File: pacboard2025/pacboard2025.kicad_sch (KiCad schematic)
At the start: 28 parts, among them J1 XT30 Male Connector, U2 D24V50F5, U3 ProS3, U6 BNO085

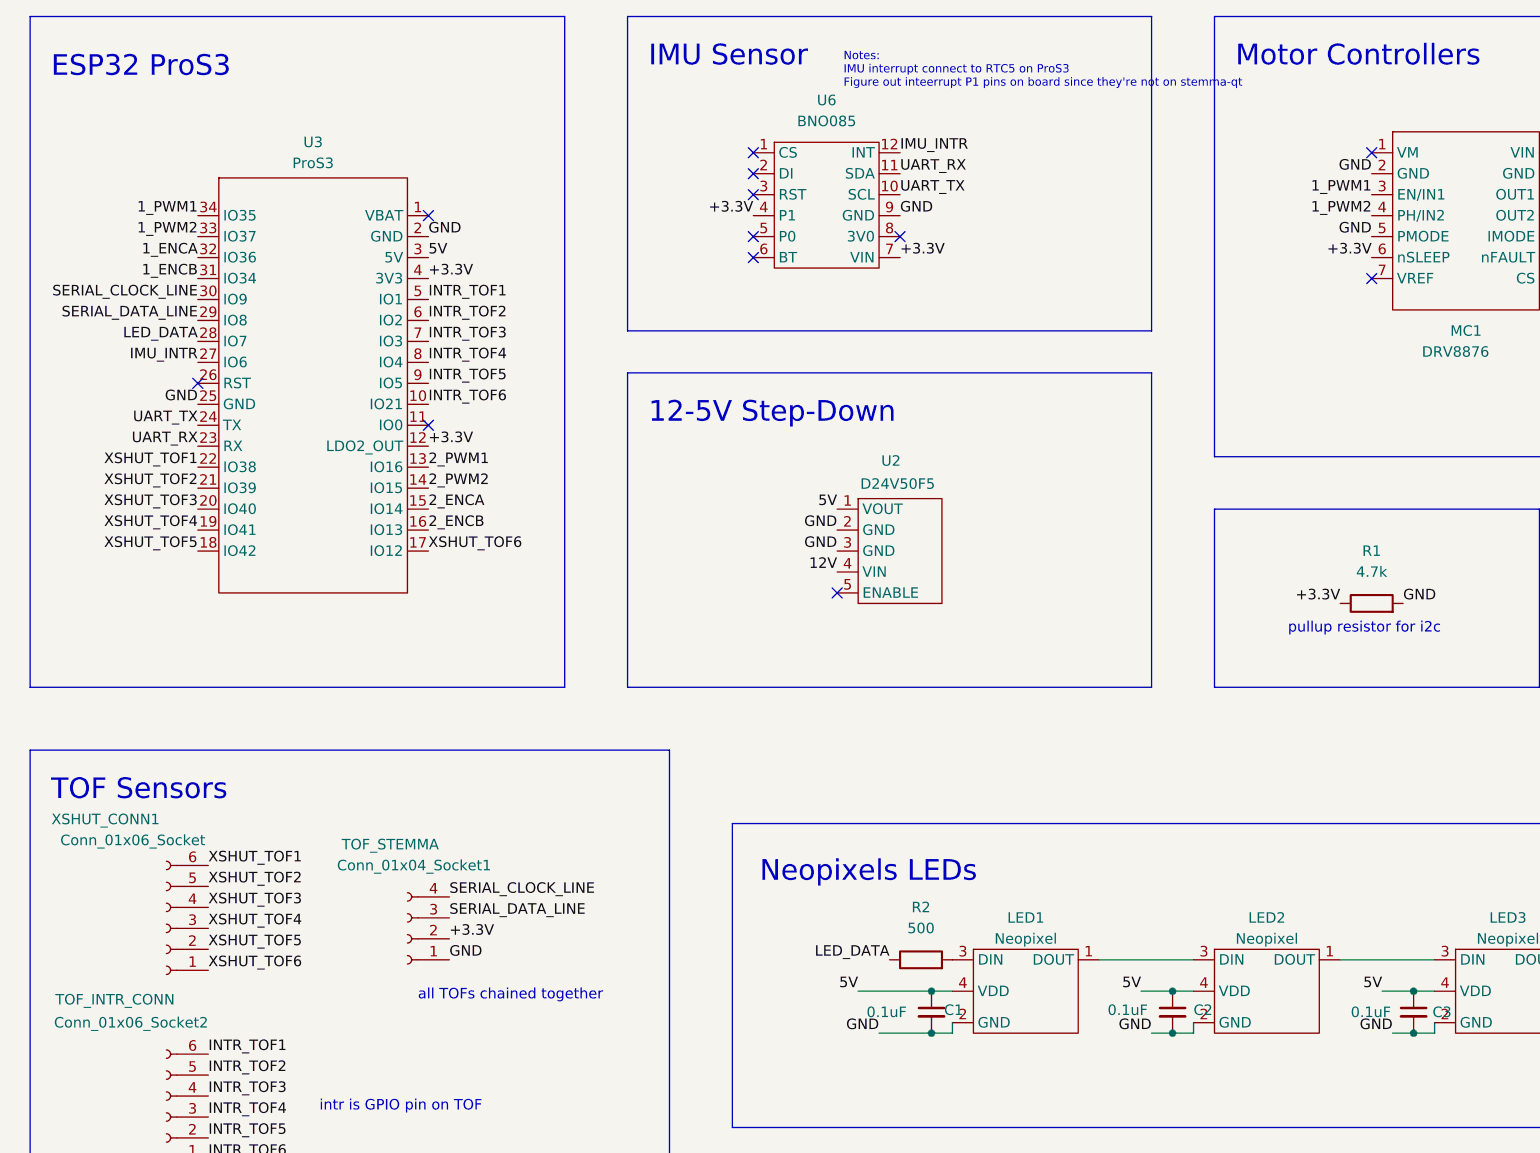
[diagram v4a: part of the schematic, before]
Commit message: changed layout
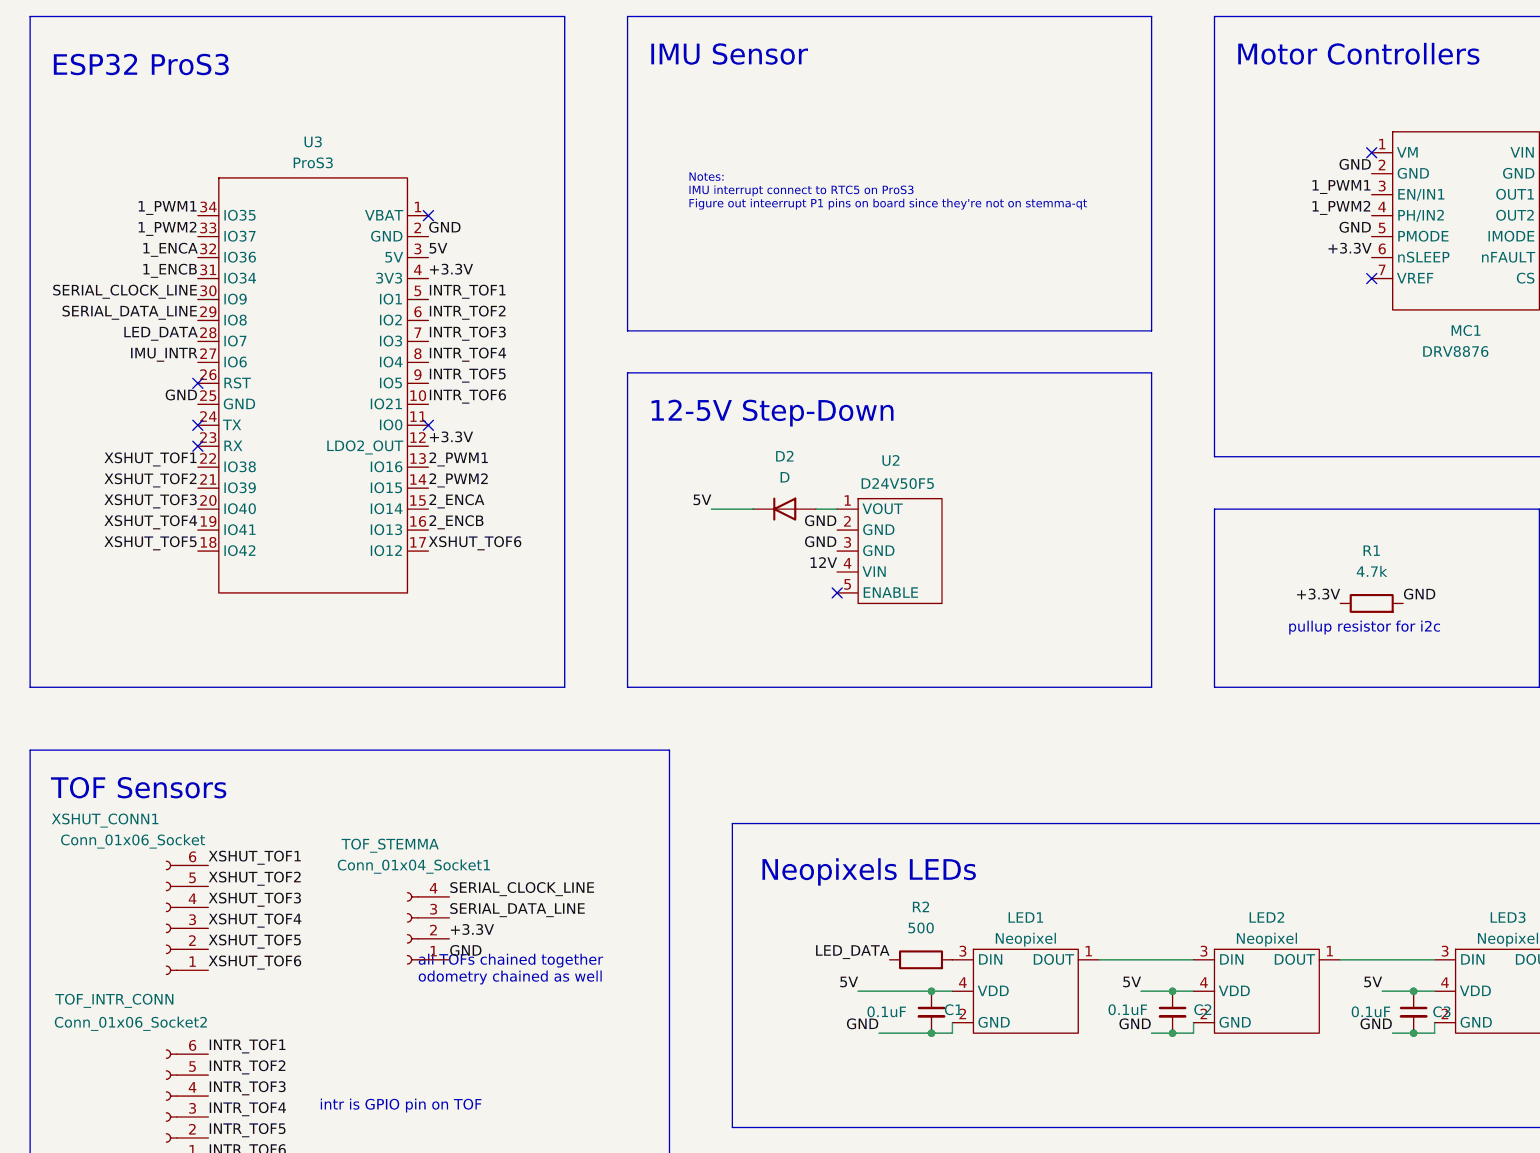
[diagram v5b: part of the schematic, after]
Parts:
- removed U6: BNO085, board1_footprints:BNU0085, symbol board1_libs:BNO085
- added D2: D, Capacitor_SMD:C_0805_2012Metric_Pad1.18x1.45mm_HandSolder, symbol Device:D
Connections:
- net 5V: now also D2.1 (K); no longer U2.1 (VOUT)
- net UART_RX: no longer names the net of U3.23 (RX)
- net UART_TX: no longer names the net of U3.24 (TX)
- new net: D2.2 (A), U2.1 (VOUT)
- no-connect marks 23 -> 19
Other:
- note added: "all TOFs chained together odometry chained as well"
- note removed: "all TOFs chained together"
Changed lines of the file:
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@@
-	)
-	(no_connect
-		(at 109.22 38.1)
 	)
 	(no_connect
@@
 	)
 	(no_connect
+		(at 41.91 71.12)
+	)
+	(no_connect
 		(at 69.85 71.12)
 	)
@@
 	)
 	(no_connect
-		(at 109.22 43.18)
-	)
-	(no_connect
 		(at 259.08 53.34)
-	)
-	(no_connect
-		(at 109.22 48.26)
 	)
 	(no_connect
@@
 	)
 	(no_connect
-		(at 127 48.26)
-	)
-	(no_connect
-		(at 109.22 40.64)
+		(at 41.91 73.66)
 	)
 	(no_connect
@@
 	)
 	(no_connect
-		(at 109.22 50.8)
-	)
-	(no_connect
 		(at 259.08 50.8)
 	)
@@
 	(wire
 		(pts
+			(xy 116.84 81.28) (xy 119.38 81.28)
+		)
+		(stroke
+			(width 0)
+			(type default)
+		)
+	)
+	(wire
+		(pts
 			(xy 214.63 139.7) (xy 218.44 139.7)
 		)
@@
 		(pts
 			(xy 124.46 144.78) (xy 130.81 144.78)
+		)
+		(stroke
+			(width 0)
+			(type default)
+		)
+	)
+	(wire
+		(pts
+			(xy 104.14 81.28) (xy 109.22 81.28)
 		)
 		(stroke
@@
 	(text "Notes:\nIMU interrupt connect to RTC5 on ProS3\nFigure out inteerrupt P1 pins on board since they're not on stemma-qt\n\n"
 		(exclude_from_sim no)
-		(at 120.142 28.956 0)
+		(at 101.346 43.688 0)
 		(effects
 			(font
@@
 		)
 	)
-	(text "all TOFs chained together\n"
+	(text "all TOFs chained together\nodometry chained as well\n\n"
 		(exclude_from_sim no)
 		(at 68.58 140.97 0)
@@
 		)
 	)
-	(label "+3.3V"
-		(at 109.22 45.72 180)
-		(fields_autoplaced yes)
-		(effects
-			(font
-				(size 1.27 1.27)
-			)
-			(justify right bottom)
-		)
-	)
 	(label "BAT_12V"
 		(at 295.91 38.1 0)
@@
 		)
 	)
-	(label "UART_TX"
-		(at 127 43.18 0)
-		(fields_autoplaced yes)
-		(effects
-			(font
-				(size 1.27 1.27)
-			)
-			(justify left bottom)
-		)
-	)
 	(label "XSHUT_TOF6"
 		(at 69.85 86.36 0)
@@
 		)
 	)
-	(label "UART_TX"
-		(at 41.91 71.12 180)
-		(fields_autoplaced yes)
-		(effects
-			(font
-				(size 1.27 1.27)
-			)
-			(justify right bottom)
-		)
-	)
-	(label "+3.3V"
-		(at 127 50.8 0)
-		(fields_autoplaced yes)
-		(effects
-			(font
-				(size 1.27 1.27)
-			)
-			(justify left bottom)
-		)
-	)
 	(label "XSHUT_TOF2"
 		(at 43.18 127 0)
@@
 		)
 	)
-	(label "IMU_INTR"
-		(at 127 38.1 0)
-		(fields_autoplaced yes)
-		(effects
-			(font
-				(size 1.27 1.27)
-			)
-			(justify left bottom)
-		)
-	)
 	(label "XSHUT_TOF6"
 		(at 43.18 137.16 0)
@@
 	)
 	(label "GND"
-		(at 127 45.72 0)
-		(fields_autoplaced yes)
-		(effects
-			(font
-				(size 1.27 1.27)
-			)
-			(justify left bottom)
-		)
-	)
-	(label "GND"
 		(at 69.85 48.26 0)
 		(fields_autoplaced yes)
@@
 		)
 	)
-	(label "UART_RX"
-		(at 127 40.64 0)
-		(fields_autoplaced yes)
-		(effects
-			(font
-				(size 1.27 1.27)
-			)
-			(justify left bottom)
-		)
-	)
 	(label "1_PWM2"
 		(at 184.15 45.72 180)
@@
 		)
 	)
-	(label "UART_RX"
-		(at 41.91 73.66 180)
-		(fields_autoplaced yes)
-		(effects
-			(font
-				(size 1.27 1.27)
-			)
-			(justify right bottom)
-		)
-	)
 	(label "SERIAL_DATA_LINE"
 		(at 41.91 58.42 180)
@@
 	)
 	(label "5V"
-		(at 119.38 81.28 180)
+		(at 104.14 81.28 180)
 		(fields_autoplaced yes)
 		(effects
@@
 	)
 	(symbol
-		(lib_id "board1_libs:BNO085")
-		(at 118.11 35.56 0)
-		(unit 1)
-		(exclude_from_sim no)
-		(in_bom yes)
-		(on_board yes)
-		(dnp no)
-		(fields_autoplaced yes)
-		(property "Reference" "U6"
-			(at 118.11 31.75 0)
-			(effects
-				(font
-					(size 1.27 1.27)
-				)
-			)
-		)
-		(property "Value" "BNO085"
-			(at 118.11 34.29 0)
-			(effects
-				(font
-					(size 1.27 1.27)
-				)
-			)
-		)
-		(property "Footprint" "board1_footprints:BNU0085"
-			(at 118.11 35.56 0)
-			(effects
-				(font
-					(size 1.27 1.27)
-				)
-				(hide yes)
-			)
-		)
-		(property "Datasheet" ""
-			(at 118.11 35.56 0)
-			(effects
-				(font
-					(size 1.27 1.27)
-				)
-				(hide yes)
-			)
-		)
-		(property "Description" ""
-			(at 118.11 35.56 0)
-			(effects
-				(font
-					(size 1.27 1.27)
-				)
-				(hide yes)
-			)
-		)
-		(pin "10"
-		)
-		(pin "11"
-		)
-		(pin "12"
-		)
-		(pin "2"
-		)
-		(pin "3"
-		)
-		(pin "4"
-		)
-		(pin "5"
-		)
-		(pin "6"
-		)
-		(pin "7"
-		)
-		(pin "8"
-		)
-		(pin "9"
-		)
-		(pin "1"
-		)
-		(instances
-			(project "pacboard2025"
-				(path "/8e380e0f-b63e-4626-b5ee-6ded4a9a683b"
-					(reference "U6")
-					(unit 1)
-				)
-			)
-		)
-	)
-	(symbol
 		(lib_id "board1_libs:DRV8876")
 		(at 193.04 36.83 0)
@@
 					(unit 1)
 				)
+			)
+		)
+	)
+	(symbol
+		(lib_id "Device:D")
+		(at 113.03 81.28 0)
+		(unit 1)
+		(exclude_from_sim no)
+		(in_bom yes)
+		(on_board yes)
+		(dnp no)
+		(fields_autoplaced yes)
+		(property "Reference" "D2"
+			(at 113.03 74.93 0)
+			(effects
+				(font
+					(size 1.27 1.27)
+				)
+			)
+		)
+		(property "Value" "D"
+			(at 113.03 77.47 0)
+			(effects
+				(font
+					(size 1.27 1.27)
+				)
+			)
+		)
+		(property "Footprint" "Capacitor_SMD:C_0805_2012Metric_Pad1.18x1.45mm_HandSolder"
+			(at 113.03 81.28 0)
+			(effects
+				(font
+					(size 1.27 1.27)
+				)
+				(hide yes)
+			)
+		)
+		(property "Datasheet" "~"
+			(at 113.03 81.28 0)
+			(effects
+				(font
+					(size 1.27 1.27)
+				)
+				(hide yes)
+			)
+		)
+		(property "Description" "Diode"
+			(at 113.03 81.28 0)
+			(effects
+				(font
+					(size 1.27 1.27)
+				)
+				(hide yes)
+			)
+		)
+		(property "Sim.Device" "D"
+			(at 113.03 81.28 0)
+			(effects
+				(font
+					(size 1.27 1.27)
+				)
+				(hide yes)
+			)
+		)
+		(property "Sim.Pins" "1=K 2=A"
+			(at 113.03 81.28 0)
+			(effects
+				(font
+					(size 1.27 1.27)
+				)
+				(hide yes)
+			)
+		)
+		(pin "2"
+		)
+		(pin "1"
+		)
+		(instances
+			(project "pacboard2025"
+				(path "/8e380e0f-b63e-4626-b5ee-6ded4a9a683b"
+					(reference "D2")
+					(unit 1)
+				)

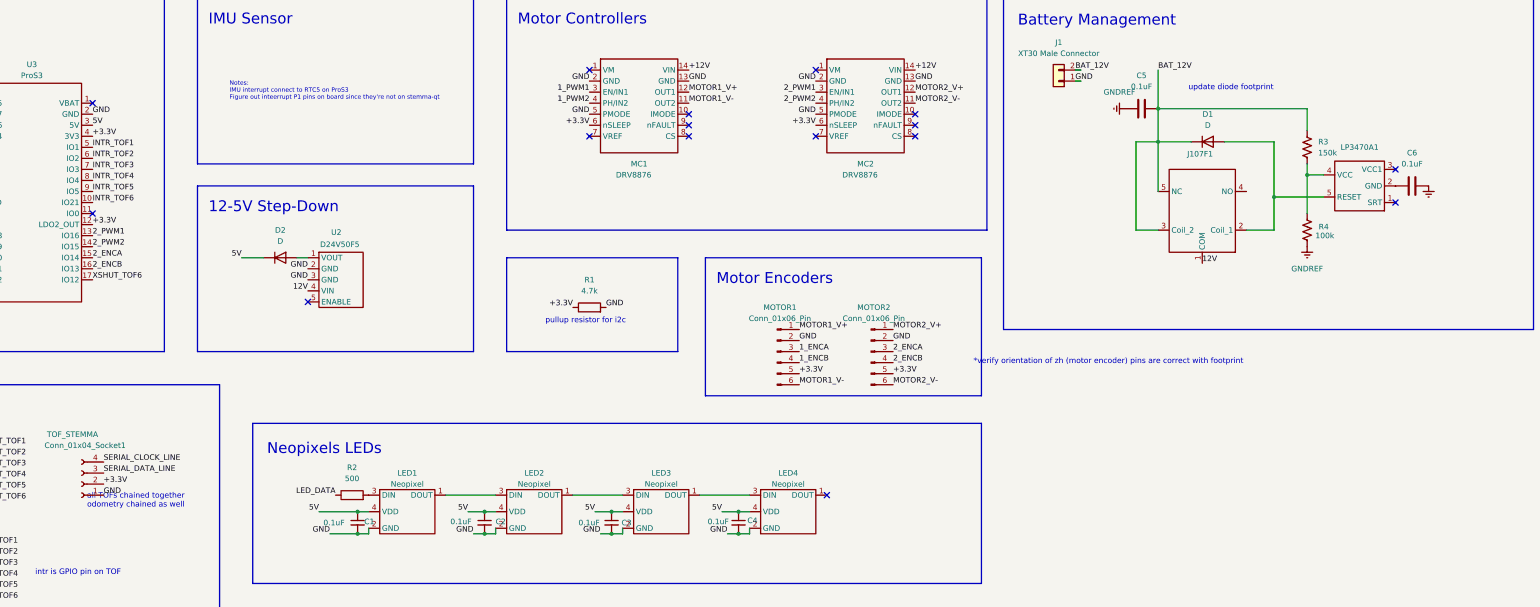
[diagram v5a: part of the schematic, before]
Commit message: layout updated
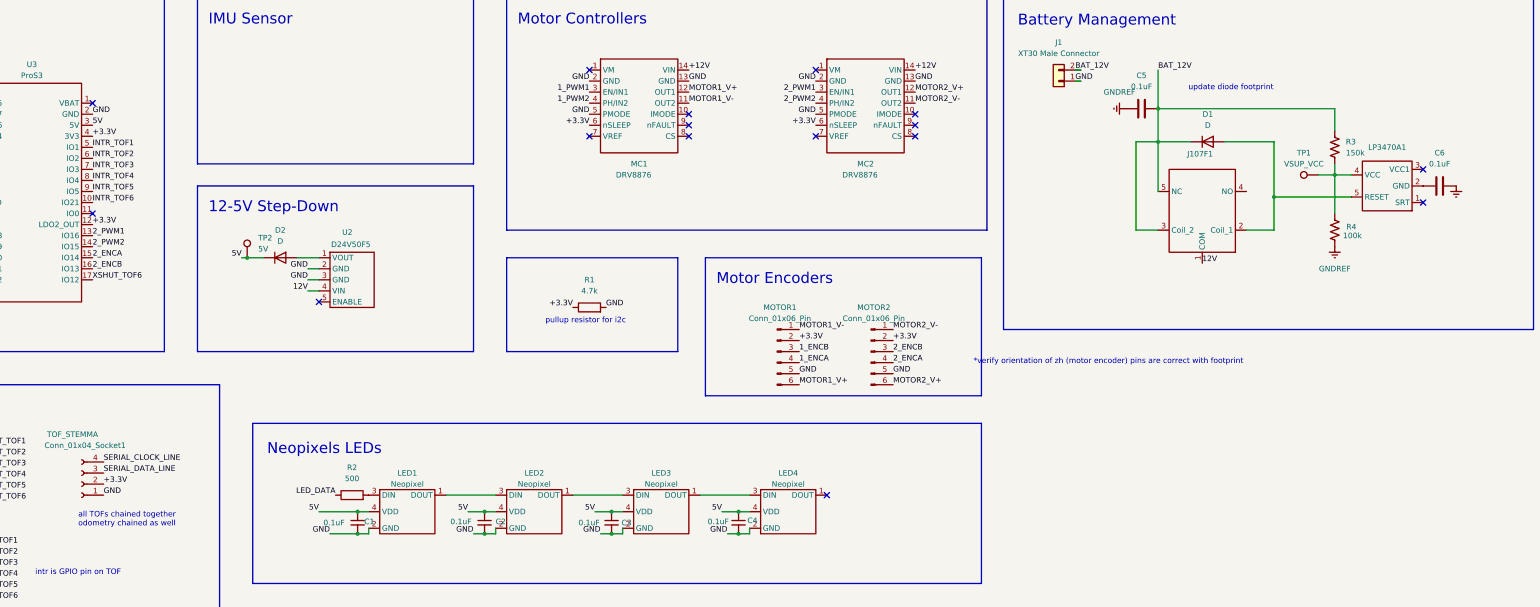
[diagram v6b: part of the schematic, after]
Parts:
- added TP1: VSUP_VCC, symbol Connector:TestPoint
- added TP2: 5V, symbol Connector:TestPoint
- D1, D2: footprint Capacitor_SMD:C_0805_2012Metric_Pad1.18x1.45mm_HandSolder -> board1_footprints:SOD-123FL
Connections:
- net +3.3V: now also MOTOR1.2 (Pin_2), MOTOR2.2 (Pin_2); no longer MOTOR1.5 (Pin_5), MOTOR2.5 (Pin_5)
- net 1_ENCA: now also MOTOR1.4 (Pin_4); no longer MOTOR1.3 (Pin_3)
- net 1_ENCB: now also MOTOR1.3 (Pin_3); no longer MOTOR1.4 (Pin_4)
- net 2_ENCA: now also MOTOR2.4 (Pin_4); no longer MOTOR2.3 (Pin_3)
- net 2_ENCB: now also MOTOR2.3 (Pin_3); no longer MOTOR2.4 (Pin_4)
- net 5V: now also TP2.1
- net GND: now also MOTOR1.5 (Pin_5), MOTOR2.5 (Pin_5); no longer MOTOR1.2 (Pin_2), MOTOR2.2 (Pin_2)
- net MOTOR1_V+: now also MOTOR1.6 (Pin_6); no longer MOTOR1.1 (Pin_1)
- net MOTOR1_V-: now also MOTOR1.1 (Pin_1); no longer MOTOR1.6 (Pin_6)
- net MOTOR2_V+: now also MOTOR2.6 (Pin_6); no longer MOTOR2.1 (Pin_1)
- net MOTOR2_V-: now also MOTOR2.1 (Pin_1); no longer MOTOR2.6 (Pin_6)
- net at LP3470A1.4 (VCC), R3.2, R4.1: now also TP1.1
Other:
- note removed: "Notes: IMU interrupt connect to RTC5 on ProS3 Figure out inteerrupt P1 pins on board since they're not on stemma-qt"
- moved on the sheet: C6, LP3470A1, R3, R4, U2

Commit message: PCB with routing
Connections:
- net +12V is gone; now on net 12V: MC1.14 (VIN), MC2.14 (VIN)
- net +3.3V: no longer U3.4 (3V3)
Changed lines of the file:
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@@
-		)
-	)
-	(label "+3.3V"
-		(at 69.85 53.34 0)
-		(fields_autoplaced yes)
-		(effects
-			(font
-				(size 1.27 1.27)
-			)
-			(justify left bottom)
 		)
 	)
@@
 		)
 	)
-	(label "+12V"
+	(label "12V"
 		(at 207.01 38.1 0)
 		(fields_autoplaced yes)
@@
 		)
 	)
-	(label "+12V"
+	(label "12V"
 		(at 259.08 38.1 0)
 		(fields_autoplaced yes)

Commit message: added testpoints
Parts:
- added TP3: GND, Connector_PinHeader_2.54mm:PinHeader_1x01_P2.54mm_Vertical, symbol Connector:TestPoint
- INTR_TOF: renamed from Conn_01x06_Socket2; value TOF_INTR_CONN -> Conn_01x06_Socket2
- TP1, TP2: footprint (none) -> Connector_PinHeader_2.54mm:PinHeader_1x01_P2.54mm_Vertical
- renumbered Conn_01x04_Socket1 to STEMMA_QT1, XSHUT_CONN1 to XSHUT_TOF
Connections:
- net GNDREF is gone; now on net GND: C5.1, C6.2, R4.2
- net GND: now also TP3.1
